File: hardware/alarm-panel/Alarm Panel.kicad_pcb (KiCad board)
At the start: 2 copper layers, 110 x 80 mm, 34 parts, among them J1 DC_BARREL_JACK, J10 W5500, J11 AUX_12V_GND, J12 AUX_12V_GND, J13 SIREN_OUT, J2 Z1_GND_Z2, J3 Z3_GND_Z4, J4 Z5_GND_Z6, J5 Z7_GND_Z8, J6 Z9_GND_Z10, J7 SPARE_NC_GND_NC, J8 PWR_MODULE, J9 ESP32_OLED, Q1 IRFZ44N, U1 TC4420CPA

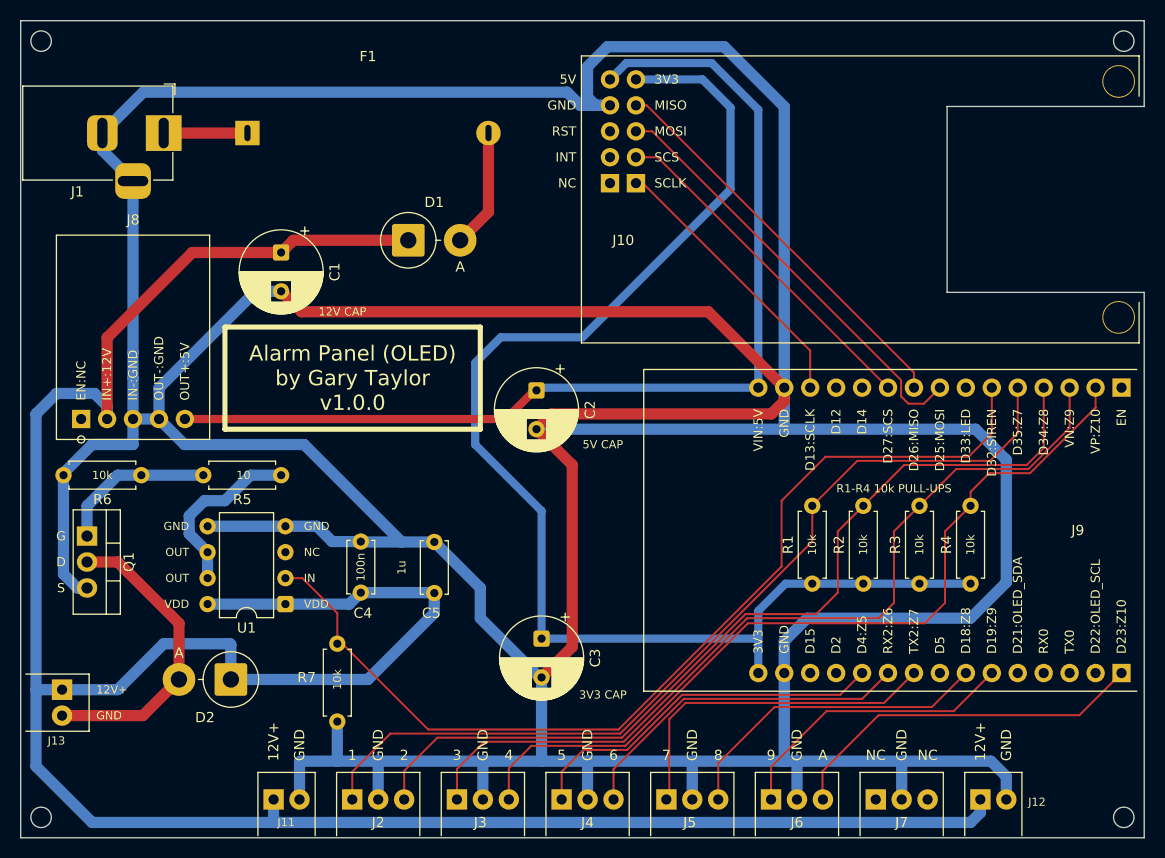
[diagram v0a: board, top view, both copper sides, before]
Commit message: Fixed Track Widths. Fixes #10.
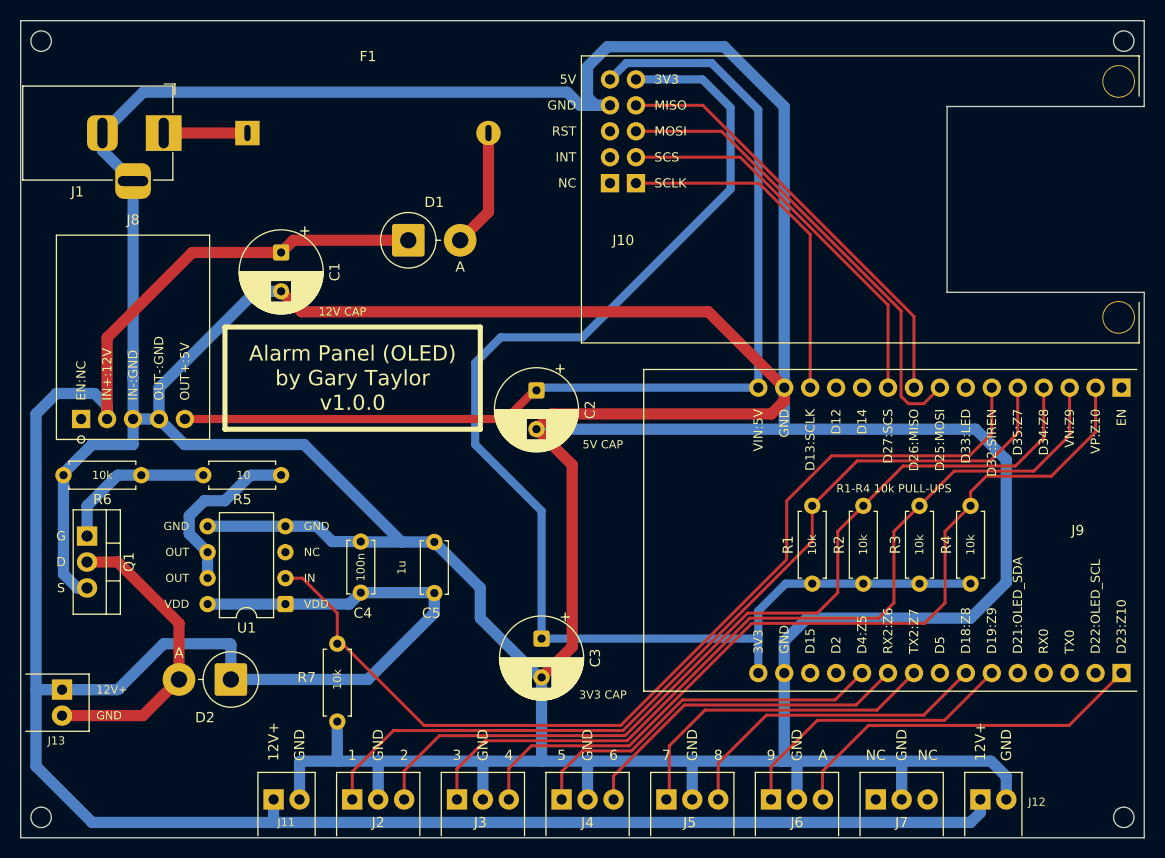
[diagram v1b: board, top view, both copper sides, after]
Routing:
- net SCLK: track 27.5 -> 34.1 mm
- net SCS: track 34.0 -> 38.8 mm
- net MOSI: track 42.4 -> 46.3 mm
- net MISO: track 39.5 -> 42.8 mm
- net Z7: track 33.8 -> 32.3 mm
- net Z4: track 82.0 -> 83.4 mm
- net SIREN_GATE: track 97.3 -> 96.6 mm
- net Z2: track 87.9 -> 87.3 mm
